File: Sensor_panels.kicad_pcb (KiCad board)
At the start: 2 copper layers, 100 x 100 mm, 232 parts, among them IC1 STM32L051K8T6, P1 CONN_02X04, P2 CONN_02X04, P3 CONN_01X02, Q1 AO3401, Q2 NMosfetGen, Q3 NMosfetGen, Q4 Q_NMOS_GSD, SW1 SW_PUSH, SW2 SW_PUSH, U1 MCP60x4, U2 HTU21D, U3 PIR, U4 TPS79718, U5 EPL3015, U6 TPS61222

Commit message: Finish layout
Signed-off-by: Philip Luyckx <philip.luyckx@gmail.com>
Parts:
- removed the C13 at (103.6, 95.6)
- removed the C13 at (153.6, 95.6)
- removed the C13 at (153.6, 45.6)
- removed the C5 at (130.4, 104.7)
- removed the C5 at (180.4, 104.7)
- removed the C5 at (180.4, 54.7)
- removed the D1 at (134.9, 127.3)
- removed the D1 at (184.9, 127.3)
- removed the D1 at (184.9, 77.3)
- removed the D2 at (97.6, 94.5)
- removed the D2 at (147.6, 94.5)
- removed the D2 at (147.6, 44.5)
- removed the P2 at (129.2, 135.2)
- removed the P2 at (179.2, 135.2)
- removed the P2 at (179.2, 85.2)
- removed the P3 at (134.7, 137.1)
- removed the P3 at (184.7, 137.1)
- removed the P3 at (184.7, 87.1)
- removed the P3 at (134.7, 87.1)
- removed the Q2 at (132.7, 99.9)
- removed the Q2 at (182.7, 99.9)
- removed the Q2 at (182.7, 49.9)
- removed the R1 at (127.6, 107.7)
- removed the R1 at (177.6, 107.7)
- removed the R1 at (177.6, 57.7)
- removed the R18 at (137.2, 99.8)
- removed the R18 at (187.2, 99.8)
- removed the R18 at (187.2, 49.9)
- removed the R4 at (138.6, 127.3)
- removed the R4 at (188.6, 127.3)
- removed the R4 at (188.6, 77.3)
- removed the SW1 at (134.8, 104.7)
- removed the SW1 at (184.8, 104.7)
- removed the SW1 at (184.8, 54.7)
- removed the SW2 at (135.0, 118.6)
- removed the SW2 at (185.0, 118.6)
- removed the SW2 at (185.0, 68.6)
- added C13: 100nF, Resistors_SMD:R_0805, F.Cu at (106.0, 96.7)
- added C13: 100nF, Resistors_SMD:R_0805, F.Cu at (156.0, 96.7)
- added C13: 100nF, Resistors_SMD:R_0805, F.Cu at (156.0, 46.7)
- added C5: 100nF, Resistors_SMD:R_0805, F.Cu at (135.8, 128.2)
- added C5: 100nF, Resistors_SMD:R_0805, F.Cu at (185.8, 128.2)
- added C5: 100nF, Resistors_SMD:R_0805, F.Cu at (185.8, 78.2)
- added D1: LED, Resistors_SMD:R_1206, B.Cu at (126.3, 119.2)
- added D1: LED, Resistors_SMD:R_1206, B.Cu at (176.3, 119.2)
- added D1: LED, Resistors_SMD:R_1206, B.Cu at (176.3, 69.2)
- added D2: PhotoDiode, CustomModules:PD638C, F.Cu at (94.2, 94.0)
- added D2: PhotoDiode, CustomModules:PD638C, F.Cu at (144.2, 94.0)
- added D2: PhotoDiode, CustomModules:PD638C, F.Cu at (144.2, 44.0)
- added P2: CONN_02X04, PinHeaders:Pin_Header_Straight_2x04_TH, F.Cu at (128.7, 133.5)
- added P2: CONN_02X04, PinHeaders:Pin_Header_Straight_2x04_TH, F.Cu at (178.7, 133.5)
- added P2: CONN_02X04, PinHeaders:Pin_Header_Straight_2x04_TH, F.Cu at (178.7, 83.5)
- added P3: CONN_01X02, ConnWago:ConnWago_2059_2P_SMD, F.Cu at (137.9, 104.3)
- added P3: CONN_01X02, ConnWago:ConnWago_2059_2P_SMD, F.Cu at (187.9, 104.3)
- added P3: CONN_01X02, ConnWago:ConnWago_2059_2P_SMD, F.Cu at (187.9, 54.4)
- added P3: CONN_01X02, ConnWago:ConnWago_2059_2P_SMD, F.Cu at (137.9, 54.4)
- added Q2: NMosfetGen, CustomSmd:SOT23, F.Cu at (132.9, 101.1)
- added Q2: NMosfetGen, CustomSmd:SOT23, F.Cu at (182.9, 101.1)
- added Q2: NMosfetGen, CustomSmd:SOT23, F.Cu at (182.9, 51.1)
- added R1: 10k, Resistors_SMD:R_0603, F.Cu at (135.8, 126.3)
- added R1: 10k, Resistors_SMD:R_0603, F.Cu at (185.8, 126.3)
- added R1: 10k, Resistors_SMD:R_0603, F.Cu at (185.8, 76.3)
- added R18: 10k, Resistors_SMD:R_0603, F.Cu at (137.4, 101.0)
- added R18: 10k, Resistors_SMD:R_0603, F.Cu at (187.4, 101.0)
- added R18: 10k, Resistors_SMD:R_0603, F.Cu at (187.4, 51.0)
- added R4: 475, Resistors_SMD:R_0603, F.Cu at (133.5, 119.2)
- added R4: 475, Resistors_SMD:R_0603, F.Cu at (183.5, 119.2)
- added R4: 475, Resistors_SMD:R_0603, F.Cu at (183.5, 69.2)
- added REF**: 1pin, Connect:1pin, F.Cu at (131.1, 93.0)
- added REF**: 1pin, Connect:1pin, F.Cu at (133.8, 99.0)
- added REF**: MountingHole_2.2mm_M2_Pad, Mounting_Holes:MountingHole_2.2mm_M2_Pad, F.Cu at (100.1, 94.2)
- added REF**: 1pin, Connect:1pin, F.Cu at (137.1, 93.0)
- added REF**: 1pin, Connect:1pin, F.Cu at (139.1, 93.0)
- added REF**: 1pin, Connect:1pin, F.Cu at (137.1, 94.3)
- added REF**: 1pin, Connect:1pin, F.Cu at (139.1, 94.3)
- added REF**: 1pin, Connect:1pin, F.Cu at (137.1, 91.8)
- added REF**: 1pin, Connect:1pin, F.Cu at (139.1, 91.8)
- added REF**: MountingHole_2.2mm_M2_Pad, Mounting_Holes:MountingHole_2.2mm_M2_Pad, F.Cu at (135.0, 112.2)
- added REF**: 1pin, Connect:1pin, F.Cu at (137.8, 99.0)
- added REF**: 1pin, Connect:1pin, F.Cu at (131.1, 94.3)
- added REF**: 1pin, Connect:1pin, F.Cu at (135.8, 99.0)
- added REF**: MountingHole_2.2mm_M2_Pad, Mounting_Holes:MountingHole_2.2mm_M2_Pad, F.Cu at (100.1, 131.2)
- added REF**: 1pin, Connect:1pin, F.Cu at (181.1, 93.0)
- added REF**: 1pin, Connect:1pin, F.Cu at (181.1, 94.3)
- added REF**: 1pin, Connect:1pin, F.Cu at (183.1, 94.3)
- added REF**: 1pin, Connect:1pin, F.Cu at (181.1, 91.8)
- added REF**: 1pin, Connect:1pin, F.Cu at (185.1, 93.0)
- added REF**: 1pin, Connect:1pin, F.Cu at (185.1, 91.8)
- added REF**: 1pin, Connect:1pin, F.Cu at (185.1, 94.3)
- added REF**: 1pin, Connect:1pin, F.Cu at (183.1, 91.8)
- added REF**: 1pin, Connect:1pin, F.Cu at (133.1, 94.3)
- added REF**: 1pin, Connect:1pin, F.Cu at (183.1, 93.0)
- added REF**: 1pin, Connect:1pin, F.Cu at (183.8, 99.0)
- added REF**: MountingHole_2.2mm_M2_Pad, Mounting_Holes:MountingHole_2.2mm_M2_Pad, F.Cu at (150.1, 94.2)
- added REF**: 1pin, Connect:1pin, F.Cu at (187.1, 93.0)
- added REF**: 1pin, Connect:1pin, F.Cu at (189.1, 93.0)
- added REF**: 1pin, Connect:1pin, F.Cu at (187.1, 94.3)
- added REF**: 1pin, Connect:1pin, F.Cu at (189.1, 94.3)
- added REF**: 1pin, Connect:1pin, F.Cu at (187.1, 91.8)
- added REF**: 1pin, Connect:1pin, F.Cu at (189.1, 91.8)
- added REF**: MountingHole_2.2mm_M2_Pad, Mounting_Holes:MountingHole_2.2mm_M2_Pad, F.Cu at (185.0, 112.2)
- added REF**: 1pin, Connect:1pin, F.Cu at (131.1, 91.8)
- added REF**: 1pin, Connect:1pin, F.Cu at (187.8, 99.0)
- added REF**: 1pin, Connect:1pin, F.Cu at (185.8, 99.0)
- added REF**: MountingHole_2.2mm_M2_Pad, Mounting_Holes:MountingHole_2.2mm_M2_Pad, F.Cu at (150.1, 131.2)
- added REF**: 1pin, Connect:1pin, F.Cu at (181.1, 43.0)
- added REF**: 1pin, Connect:1pin, F.Cu at (181.1, 44.3)
- added REF**: 1pin, Connect:1pin, F.Cu at (183.1, 44.3)
- added REF**: 1pin, Connect:1pin, F.Cu at (181.1, 41.8)
- added REF**: 1pin, Connect:1pin, F.Cu at (185.1, 43.0)
- added REF**: 1pin, Connect:1pin, F.Cu at (185.1, 41.8)
- added REF**: 1pin, Connect:1pin, F.Cu at (185.1, 44.3)
- added REF**: 1pin, Connect:1pin, F.Cu at (135.1, 93.0)
- added REF**: 1pin, Connect:1pin, F.Cu at (183.1, 41.8)
- added REF**: 1pin, Connect:1pin, F.Cu at (183.1, 43.0)
- added REF**: 1pin, Connect:1pin, F.Cu at (183.8, 49.0)
- added REF**: MountingHole_2.2mm_M2_Pad, Mounting_Holes:MountingHole_2.2mm_M2_Pad, F.Cu at (150.1, 44.2)
- added REF**: 1pin, Connect:1pin, F.Cu at (187.1, 43.0)
- added REF**: 1pin, Connect:1pin, F.Cu at (189.1, 43.0)
- added REF**: 1pin, Connect:1pin, F.Cu at (187.1, 44.3)
- added REF**: 1pin, Connect:1pin, F.Cu at (189.1, 44.3)
- added REF**: 1pin, Connect:1pin, F.Cu at (187.1, 41.8)
- added REF**: 1pin, Connect:1pin, F.Cu at (189.1, 41.8)
- added REF**: 1pin, Connect:1pin, F.Cu at (135.1, 91.8)
- added REF**: MountingHole_2.2mm_M2_Pad, Mounting_Holes:MountingHole_2.2mm_M2_Pad, F.Cu at (185.0, 62.2)
- added REF**: 1pin, Connect:1pin, F.Cu at (187.8, 49.0)
- added REF**: 1pin, Connect:1pin, F.Cu at (185.8, 49.0)
- added REF**: MountingHole_2.2mm_M2_Pad, Mounting_Holes:MountingHole_2.2mm_M2_Pad, F.Cu at (150.1, 81.2)
- added REF**: 1pin, Connect:1pin, F.Cu at (137.1, 44.3)
- added REF**: 1pin, Connect:1pin, F.Cu at (139.1, 44.3)
- added REF**: 1pin, Connect:1pin, F.Cu at (131.1, 44.3)
- added REF**: 1pin, Connect:1pin, F.Cu at (135.1, 44.3)
- added REF**: 1pin, Connect:1pin, F.Cu at (133.1, 44.3)
- added REF**: 1pin, Connect:1pin, F.Cu at (137.1, 41.8)
- added REF**: 1pin, Connect:1pin, F.Cu at (135.1, 94.3)
- added REF**: 1pin, Connect:1pin, F.Cu at (139.1, 41.8)
- added REF**: 1pin, Connect:1pin, F.Cu at (131.1, 41.8)
- added REF**: 1pin, Connect:1pin, F.Cu at (135.1, 41.8)
- added REF**: 1pin, Connect:1pin, F.Cu at (133.1, 41.8)
- added REF**: 1pin, Connect:1pin, F.Cu at (139.1, 43.0)
- added REF**: 1pin, Connect:1pin, F.Cu at (137.1, 43.0)
- added REF**: 1pin, Connect:1pin, F.Cu at (131.1, 43.0)
- added REF**: 1pin, Connect:1pin, F.Cu at (133.1, 43.0)
- added REF**: 1pin, Connect:1pin, F.Cu at (135.1, 43.0)
- added REF**: 1pin, Connect:1pin, F.Cu at (137.8, 49.0)
- added REF**: 1pin, Connect:1pin, F.Cu at (133.1, 91.8)
- added REF**: 1pin, Connect:1pin, F.Cu at (135.8, 49.0)
- added REF**: 1pin, Connect:1pin, F.Cu at (133.8, 49.0)
- added REF**: MountingHole_2.2mm_M2_Pad, Mounting_Holes:MountingHole_2.2mm_M2_Pad, F.Cu at (100.1, 44.2)
- added REF**: MountingHole_2.2mm_M2_Pad, Mounting_Holes:MountingHole_2.2mm_M2_Pad, F.Cu at (135.0, 62.2)
- added REF**: MountingHole_2.2mm_M2_Pad, Mounting_Holes:MountingHole_2.2mm_M2_Pad, F.Cu at (100.1, 81.2)
- added REF**: 1pin, Connect:1pin, F.Cu at (133.1, 93.0)
- added SW1: SW_PUSH, CustomSmd:MicroSwitch_6x6mm, F.Cu at (135.8, 132.3)
- added SW1: SW_PUSH, CustomSmd:MicroSwitch_6x6mm, F.Cu at (185.8, 132.3)
- added SW1: SW_PUSH, CustomSmd:MicroSwitch_6x6mm, F.Cu at (185.8, 82.3)
- added SW2: SW_PUSH, CustomSmd:MicroSwitch_6x6mm, F.Cu at (135.8, 120.3)
- added SW2: SW_PUSH, CustomSmd:MicroSwitch_6x6mm, F.Cu at (185.8, 120.3)
- added SW2: SW_PUSH, CustomSmd:MicroSwitch_6x6mm, F.Cu at (185.8, 70.3)
- R1: value 100k -> 10k
- R4: moved to F.Cu
- moved SW1 27.6 mm to (135.8, 82.3), turned to 90 degrees
- moved C5 24.1 mm to (135.8, 78.2), turned to 0 degrees
- moved R1 20.3 mm to (135.8, 76.3), turned to 180 degrees
- moved D1 11.8 mm to (126.3, 69.2)
- moved R4 9.57 mm to (133.5, 69.2)
- moved D2 3.43 mm to (94.2, 44.0), turned to 90 degrees
- moved C13 2.64 mm to (106.0, 46.7), turned to 270 degrees
- moved SW2 1.90 mm to (135.8, 70.3), turned to 90 degrees
- moved P2 1.71 mm to (128.7, 83.5)
- moved Q2 1.21 mm to (132.9, 51.1)
- moved R18 1.21 mm to (137.4, 51.0)
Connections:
- P2 pad 1: GND -> +BATT
- P2 pad 2: +BATT -> GND
- P2 pad 3: UART_TX -> SWDCLK
- P2 pad 4: SWDCLK -> UART_TX
- P2 pad 5: UART_RX -> SWDIO
- P2 pad 6: SWDIO -> UART_RX
- P2 pad 7: Net-(P2-Pad7) -> MCU_RST
- P2 pad 8: MCU_RST -> Net-(P2-Pad8)
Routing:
- net +BATT: track 720.9 -> 788.1 mm, vias 24 -> 12
- net MCU_LED: track 68.2 -> 13.9 mm
- net UART_RX: track 92.6 -> 52.1 mm, vias 4 -> 0
- net UART_TX: track 102.2 -> 63.6 mm
- net GND: track 509.8 -> 478.8 mm, vias 48 -> 52
- net SWDCLK: track 58.7 -> 83.8 mm, vias 8 -> 0
- net +1V8: track 427.2 -> 410.8 mm, vias 20 -> 24
- net MCU_RST: track 195.3 -> 180.5 mm, vias 16 -> 12
- net Net-(D1-Pad2): track 6.00 -> 20.0 mm, vias 0 -> 4
- net Net-(D2-Pad1): track 45.3 -> 33.0 mm
- net BTN_User: track 74.7 -> 85.9 mm, vias 0 -> 8
- net Net-(C13-Pad1): track 52.7 -> 63.6 mm
- net HTU21_SDA: track 23.7 -> 31.8 mm
- net ADC_Light: track 131.4 -> 124.0 mm
- net SWDIO: track 63.9 -> 70.9 mm, vias 8 -> 0
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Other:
- board size 100 x 100 mm -> 101 x 101.5 mm
- board text added: "GND"
- board text added: "RST"
- board text added: "USR"
- board text added: "V+"
- board text added: "V-cut"

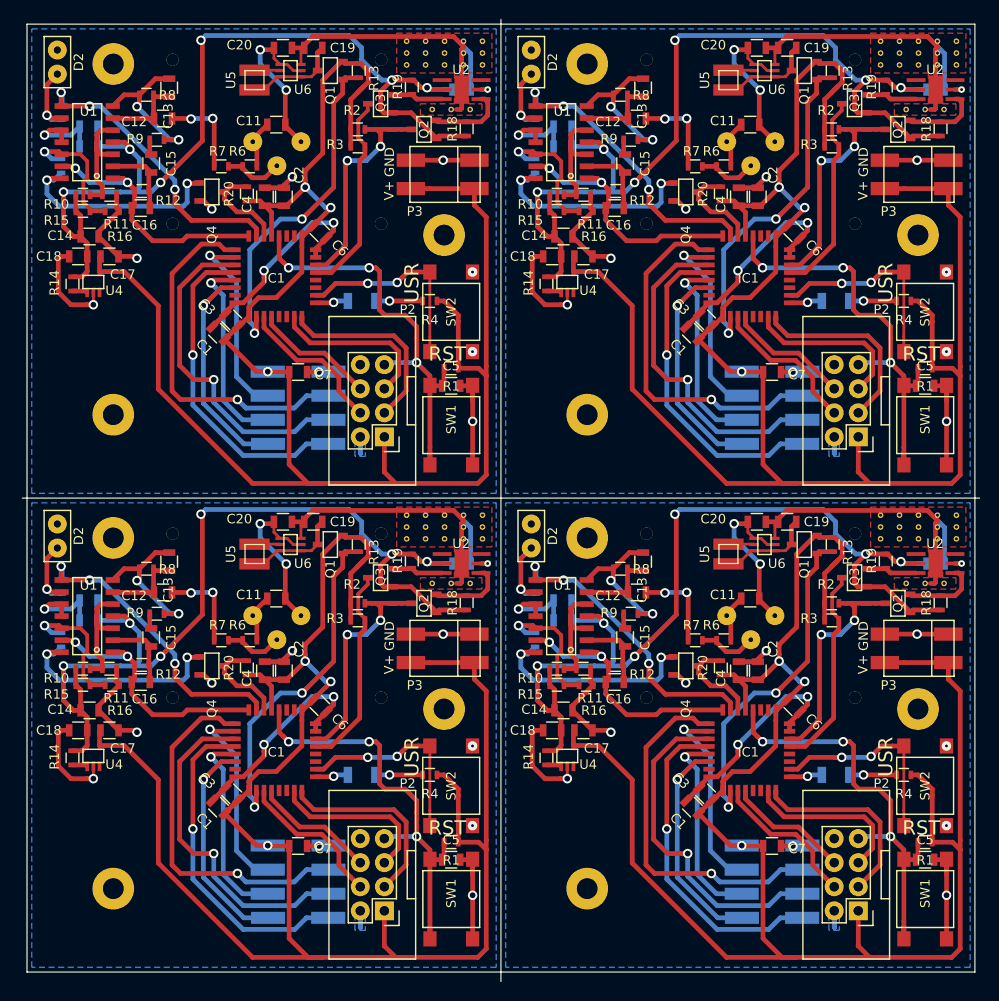
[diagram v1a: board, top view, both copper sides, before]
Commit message: Add url to open source project on silkscreens
Signed-off-by: Philip Luyckx <philip.luyckx@gmail.com>
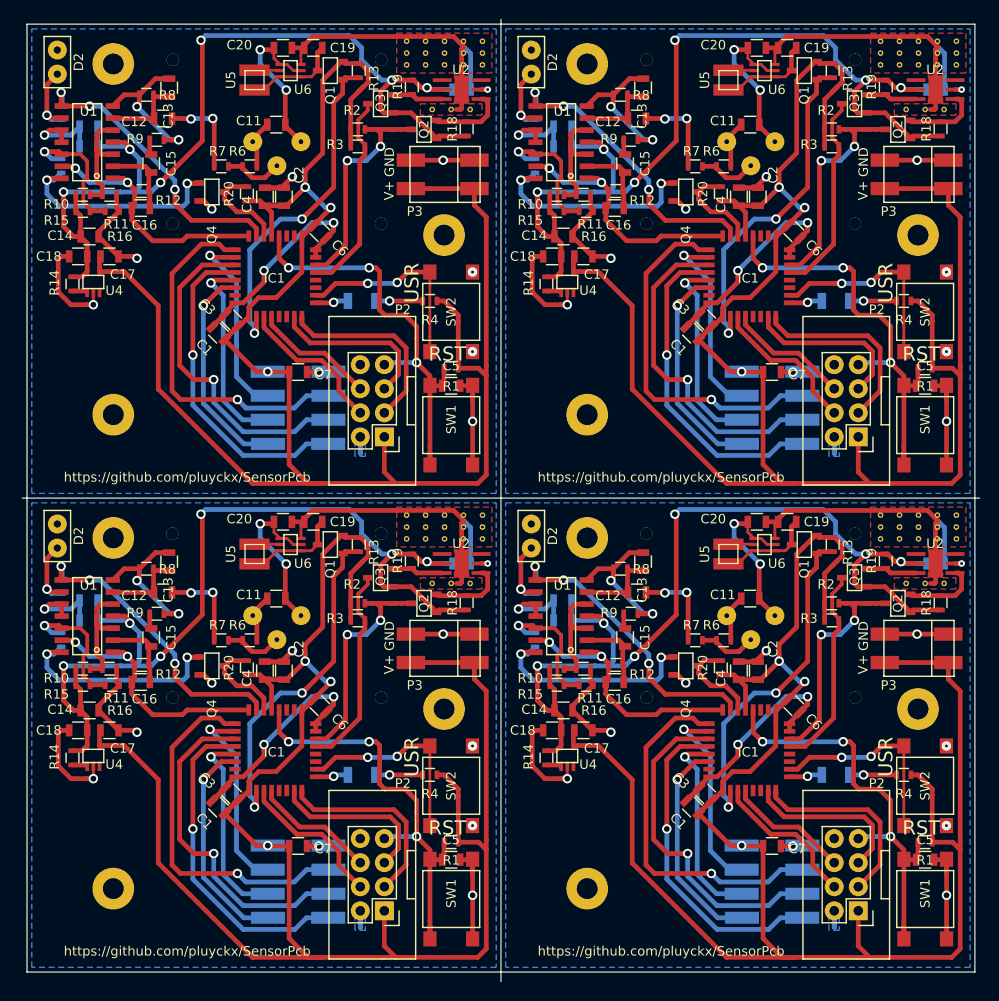
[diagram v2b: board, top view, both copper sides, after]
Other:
- board text added: "https://github.com/pluyckx/SensorPcb"
